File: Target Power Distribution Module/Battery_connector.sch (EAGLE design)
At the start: 2 parts

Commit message: Test text
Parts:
- added U$1: TACTILE-SWITCH-PTH, GeekAmmo:TACTILE-SWITCH-PTH
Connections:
- new net N$1: U$1.3, U$1.4
- net 3.7V: now also U$1.1, U$1.2
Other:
- note added: "TEST"
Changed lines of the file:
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@@
 <part name="GND-ISO2" library="SparkFun-Aesthetics" deviceset="GND-ISO" device=""/>
 <part name="3.7V1" library="SparkFun-Aesthetics" deviceset="VCC" device="" value="3.7V"/>
+<part name="U$1" library="GeekAmmo" deviceset="TACTILE-SWITCH" device="-PTH"/>
 </parts>
 <sheets>
 <sheet>
 <plain>
-<text x="99.06" y="55.88" size="1.778" layer="91">Overvoltage Protection</text>
+<text x="99.06" y="53.34" size="1.778" layer="91">Overvoltage Protection</text>
 <rectangle x1="93.98" y1="35.56" x2="127" y2="68.58" layer="94"/>
+<text x="48.26" y="78.74" size="1.778" layer="91">TEST</text>
 </plain>
 <instances>
@@
 <instance part="GND-ISO2" gate="G$1" x="71.12" y="40.64"/>
 <instance part="3.7V1" gate="G$1" x="71.12" y="68.58"/>
+<instance part="U$1" gate="G$1" x="81.28" y="60.96" smashed="yes">
+<attribute name="NAME" x="77.216" y="66.548" size="1.778" layer="95"/>
+</instance>
 </instances>
 <busses>
@@
 <wire x1="71.12" y1="55.88" x2="71.12" y2="68.58" width="0.1524" layer="91"/>
 <pinref part="3.7V1" gate="G$1" pin="VCC"/>
-<wire x1="71.12" y1="55.88" x2="93.98" y2="55.88" width="0.1524" layer="91"/>
+<pinref part="U$1" gate="G$1" pin="2"/>
+<wire x1="71.12" y1="55.88" x2="76.2" y2="55.88" width="0.1524" layer="91"/>
+<wire x1="76.2" y1="55.88" x2="76.2" y2="58.42" width="0.1524" layer="91"/>
 <junction x="71.12" y="55.88"/>
+<pinref part="U$1" gate="G$1" pin="1"/>
+<wire x1="76.2" y1="58.42" x2="76.2" y2="60.96" width="0.1524" layer="91"/>
+<junction x="76.2" y="58.42"/>
 </segment>
 </net>
+<net name="N$1" class="0">
+<segment>
+<pinref part="U$1" gate="G$1" pin="3"/>
+<pinref part="U$1" gate="G$1" pin="4"/>
+<wire x1="86.36" y1="60.96" x2="86.36" y2="58.42" width="0.1524" layer="91"/>
+<wire x1="86.36" y1="58.42" x2="86.36" y2="55.88" width="0.1524" layer="91"/>
+<junction x="86.36" y="58.42"/>
+<wire x1="86.36" y1="55.88" x2="93.98" y2="55.88" width="0.1524" layer="91"/>
+</segment>
+</net>

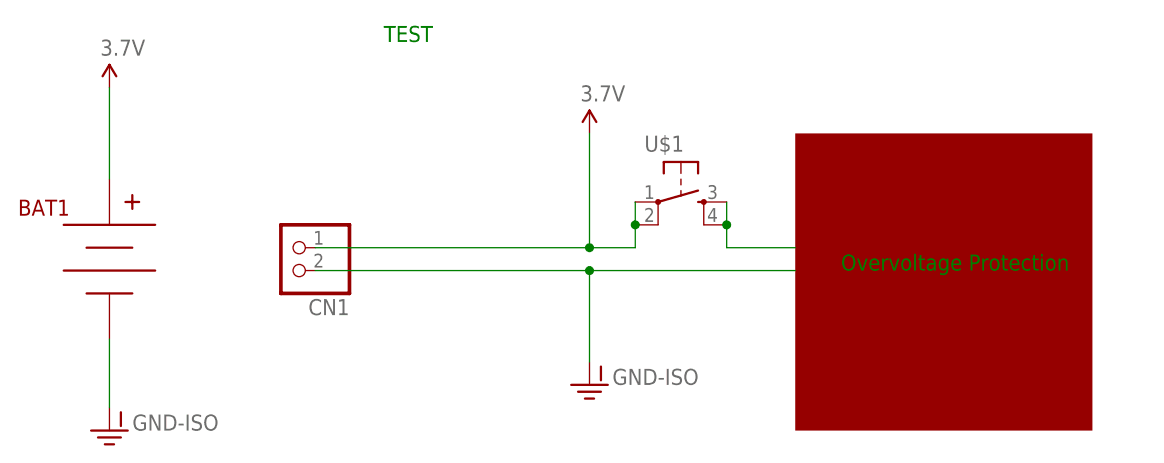
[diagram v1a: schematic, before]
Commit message: Added voltage regulator that assumes 5V battery pack
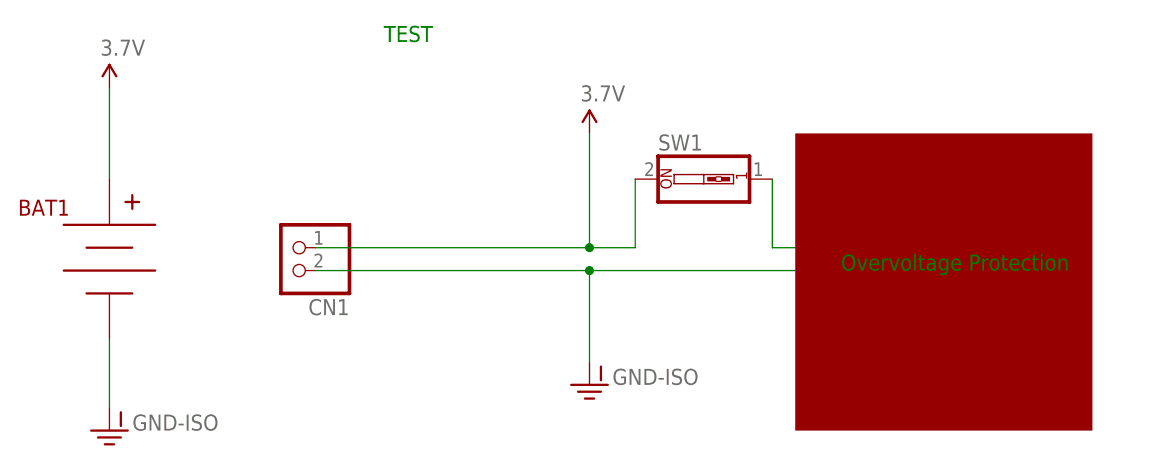
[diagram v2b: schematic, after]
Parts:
- removed U$1: TACTILE-SWITCH-PTH, GeekAmmo:TACTILE-SWITCH-PTH
- added SW1: (no value), special:SW_DIP-1
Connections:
- net 3.7V: now also SW1.2; no longer U$1.1, U$1.2
- net N$1: now also SW1.1; no longer U$1.3, U$1.4
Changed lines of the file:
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@@
 <part name="GND-ISO2" library="SparkFun-Aesthetics" deviceset="GND-ISO" device=""/>
 <part name="3.7V1" library="SparkFun-Aesthetics" deviceset="VCC" device="" value="3.7V"/>
-<part name="U$1" library="GeekAmmo" deviceset="TACTILE-SWITCH" device="-PTH"/>
+<part name="SW1" library="special" deviceset="SW_DIP-1" device=""/>
 </parts>
 <sheets>
@@
 <instance part="GND-ISO2" gate="G$1" x="71.12" y="40.64"/>
 <instance part="3.7V1" gate="G$1" x="71.12" y="68.58"/>
-<instance part="U$1" gate="G$1" x="81.28" y="60.96" smashed="yes">
-<attribute name="NAME" x="77.216" y="66.548" size="1.778" layer="95"/>
-</instance>
+<instance part="SW1" gate="G$1" x="83.82" y="63.5"/>
 </instances>
 <busses>
@@
 <wire x1="71.12" y1="55.88" x2="71.12" y2="68.58" width="0.1524" layer="91"/>
 <pinref part="3.7V1" gate="G$1" pin="VCC"/>
-<pinref part="U$1" gate="G$1" pin="2"/>
 <wire x1="71.12" y1="55.88" x2="76.2" y2="55.88" width="0.1524" layer="91"/>
-<wire x1="76.2" y1="55.88" x2="76.2" y2="58.42" width="0.1524" layer="91"/>
 <junction x="71.12" y="55.88"/>
-<pinref part="U$1" gate="G$1" pin="1"/>
-<wire x1="76.2" y1="58.42" x2="76.2" y2="60.96" width="0.1524" layer="91"/>
-<junction x="76.2" y="58.42"/>
+<pinref part="SW1" gate="G$1" pin="2"/>
+<wire x1="76.2" y1="55.88" x2="76.2" y2="63.5" width="0.1524" layer="91"/>
 </segment>
 </net>
 <net name="N$1" class="0">
 <segment>
-<pinref part="U$1" gate="G$1" pin="3"/>
-<pinref part="U$1" gate="G$1" pin="4"/>
-<wire x1="86.36" y1="60.96" x2="86.36" y2="58.42" width="0.1524" layer="91"/>
-<wire x1="86.36" y1="58.42" x2="86.36" y2="55.88" width="0.1524" layer="91"/>
-<junction x="86.36" y="58.42"/>
-<wire x1="86.36" y1="55.88" x2="93.98" y2="55.88" width="0.1524" layer="91"/>
+<pinref part="SW1" gate="G$1" pin="1"/>
+<wire x1="91.44" y1="55.88" x2="93.98" y2="55.88" width="0.1524" layer="91"/>
+<wire x1="91.44" y1="63.5" x2="91.44" y2="55.88" width="0.1524" layer="91"/>
 </segment>
 </net>
